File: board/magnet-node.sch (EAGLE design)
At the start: 19 parts, among them X1 SMA-142-0701-801/806

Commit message: started pcb
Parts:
- added C10, C11, C9: (no value), rcl:C-EUC0603
- added LED1: (no value), led:LEDSMT1206
- added R1, R2, R3: (no value), rcl:R-EU_R0603
- added SV2, SV3: (no value), con-lstb:MA07-1
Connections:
- removed net N$1: SV1.4, U$1.RST
- new net N$12: C10.2, R2.2, SV3.1, SV3.2, SV3.3, SV3.4, SV3.5, SV3.6, SV3.7, U$1.P1.3
- new net N$13: C11.2, LED1.A, R1.2, U$1.P1.5
- new net N$15: C9.2, R3.1, SV1.4, U$1.RST
- net +3V3: now also LED1.C, R3.2, SV2.1, SV2.2, SV2.3, SV2.4, SV2.5, SV2.6, SV2.7
- net GND: now also C10.1, C11.1, C9.1, R1.1, R2.1
- net N$6: now also U$2.SDA
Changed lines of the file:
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@@
 <?xml version="1.0" encoding="utf-8"?>
 <!DOCTYPE eagle SYSTEM "eagle.dtd">
-<eagle version="7.1.0">
+<eagle version="6.5.0">
 <drawing>
 <settings>
@@
 <part name="X1" library="con-coax" deviceset="SMA-" device="142-0701-801/806"/>
 <part name="GND13" library="supply1" deviceset="GND" device=""/>
+<part name="SV2" library="con-lstb" deviceset="MA07-1" device=""/>
+<part name="SV3" library="con-lstb" deviceset="MA07-1" device=""/>
+<part name="R1" library="rcl" deviceset="R-EU_" device="R0603"/>
+<part name="R2" library="rcl" deviceset="R-EU_" device="R0603"/>
+<part name="LED1" library="led" deviceset="LED" device="SMT1206"/>
+<part name="+3V6" library="supply1" deviceset="+3V3" device=""/>
+<part name="GND14" library="supply1" deviceset="GND" device=""/>
+<part name="GND15" library="supply1" deviceset="GND" device=""/>
+<part name="+3V7" library="supply1" deviceset="+3V3" device=""/>
+<part name="R3" library="rcl" deviceset="R-EU_" device="R0603"/>
+<part name="C9" library="rcl" deviceset="C-EU" device="C0603"/>
+<part name="GND16" library="supply1" deviceset="GND" device=""/>
+<part name="+3V8" library="supply1" deviceset="+3V3" device=""/>
+<part name="C10" library="rcl" deviceset="C-EU" device="C0603"/>
+<part name="C11" library="rcl" deviceset="C-EU" device="C0603"/>
 </parts>
 <sheets>
@@
 <instance part="X1" gate="G1" x="205.74" y="45.72" rot="MR0"/>
 <instance part="GND13" gate="1" x="203.2" y="40.64"/>
+<instance part="SV2" gate="1" x="86.36" y="81.28" rot="R180"/>
+<instance part="SV3" gate="1" x="88.9" y="81.28"/>
+<instance part="R1" gate="G$1" x="68.58" y="22.86" rot="R90"/>
+<instance part="R2" gate="G$1" x="73.66" y="22.86" rot="R90"/>
+<instance part="LED1" gate="G$1" x="68.58" y="58.42" rot="R180"/>
+<instance part="+3V6" gate="G$1" x="68.58" y="68.58"/>
+<instance part="GND14" gate="1" x="73.66" y="15.24"/>
+<instance part="GND15" gate="1" x="68.58" y="15.24"/>
+<instance part="+3V7" gate="G$1" x="78.74" y="96.52"/>
+<instance part="R3" gate="G$1" x="15.24" y="58.42" rot="R90"/>
+<instance part="C9" gate="G$1" x="15.24" y="38.1" rot="R180"/>
+<instance part="GND16" gate="1" x="15.24" y="33.02"/>
+<instance part="+3V8" gate="G$1" x="15.24" y="66.04"/>
+<instance part="C10" gate="G$1" x="78.74" y="22.86" rot="R180"/>
+<instance part="C11" gate="G$1" x="63.5" y="22.86" rot="R180"/>
 </instances>
 <busses>
@@
 <pinref part="GND13" gate="1" pin="GND"/>
 </segment>
+<segment>
+<pinref part="R2" gate="G$1" pin="1"/>
+<pinref part="GND14" gate="1" pin="GND"/>
+<pinref part="C10" gate="G$1" pin="1"/>
+<wire x1="78.74" y1="20.32" x2="78.74" y2="17.78" width="0.1524" layer="91"/>
+<wire x1="78.74" y1="17.78" x2="73.66" y2="17.78" width="0.1524" layer="91"/>
+<junction x="73.66" y="17.78"/>
+</segment>
+<segment>
+<pinref part="R1" gate="G$1" pin="1"/>
+<pinref part="GND15" gate="1" pin="GND"/>
+<pinref part="C11" gate="G$1" pin="1"/>
+<wire x1="63.5" y1="20.32" x2="63.5" y2="17.78" width="0.1524" layer="91"/>
+<wire x1="63.5" y1="17.78" x2="68.58" y2="17.78" width="0.1524" layer="91"/>
+<junction x="68.58" y="17.78"/>
+</segment>
+<segment>
+<pinref part="C9" gate="G$1" pin="1"/>
+<pinref part="GND16" gate="1" pin="GND"/>
+</segment>
 </net>
 <net name="+3V3" class="0">
@@
 <pinref part="+3V5" gate="G$1" pin="+3V3"/>
 </segment>
-</net>
-<net name="N$1" class="0">
-<segment>
-<pinref part="U$1" gate="G$1" pin="RST"/>
-<wire x1="25.4" y1="48.26" x2="22.86" y2="48.26" width="0.1524" layer="91"/>
-<wire x1="22.86" y1="48.26" x2="22.86" y2="50.8" width="0.1524" layer="91"/>
-<wire x1="22.86" y1="50.8" x2="5.08" y2="50.8" width="0.1524" layer="91"/>
-<pinref part="SV1" gate="1" pin="4"/>
+<segment>
+<pinref part="+3V6" gate="G$1" pin="+3V3"/>
+<pinref part="LED1" gate="G$1" pin="C"/>
+<wire x1="68.58" y1="66.04" x2="68.58" y2="63.5" width="0.1524" layer="91"/>
+</segment>
+<segment>
+<pinref part="SV2" gate="1" pin="7"/>
+<wire x1="78.74" y1="73.66" x2="78.74" y2="76.2" width="0.1524" layer="91"/>
+<pinref part="SV2" gate="1" pin="6"/>
+<junction x="78.74" y="76.2"/>
+<wire x1="78.74" y1="76.2" x2="78.74" y2="78.74" width="0.1524" layer="91"/>
+<pinref part="SV2" gate="1" pin="5"/>
+<junction x="78.74" y="78.74"/>
+<wire x1="78.74" y1="78.74" x2="78.74" y2="81.28" width="0.1524" layer="91"/>
+<pinref part="SV2" gate="1" pin="4"/>
+<junction x="78.74" y="81.28"/>
+<wire x1="78.74" y1="81.28" x2="78.74" y2="83.82" width="0.1524" layer="91"/>
+<pinref part="SV2" gate="1" pin="3"/>
+<junction x="78.74" y="83.82"/>
+<wire x1="78.74" y1="83.82" x2="78.74" y2="86.36" width="0.1524" layer="91"/>
+<pinref part="SV2" gate="1" pin="2"/>
+<junction x="78.74" y="86.36"/>
+<wire x1="78.74" y1="86.36" x2="78.74" y2="88.9" width="0.1524" layer="91"/>
+<pinref part="SV2" gate="1" pin="1"/>
+<junction x="78.74" y="88.9"/>
+<wire x1="78.74" y1="88.9" x2="78.74" y2="93.98" width="0.1524" layer="91"/>
+<pinref part="+3V7" gate="G$1" pin="+3V3"/>
+</segment>
+<segment>
+<pinref part="R3" gate="G$1" pin="2"/>
+<pinref part="+3V8" gate="G$1" pin="+3V3"/>
 </segment>
 </net>
@@
 <net name="N$6" class="0">
 <segment>
-<wire x1="83.82" y1="45.72" x2="127" y2="45.72" width="0.1524" layer="91"/>
+<wire x1="83.82" y1="45.72" x2="121.92" y2="45.72" width="0.1524" layer="91"/>
+<wire x1="121.92" y1="45.72" x2="124.46" y2="45.72" width="0.1524" layer="91"/>
 <wire x1="83.82" y1="33.02" x2="83.82" y2="45.72" width="0.1524" layer="91"/>
 <pinref part="U$1" gate="G$1" pin="P1.7"/>
 <wire x1="63.5" y1="33.02" x2="83.82" y2="33.02" width="0.1524" layer="91"/>
+<pinref part="U$2" gate="G$1" pin="SDA"/>
+<wire x1="127" y1="45.72" x2="124.46" y2="45.72" width="0.1524" layer="91"/>
 </segment>
 </net>
@@
 </segment>
 </net>
+<net name="N$12" class="0">
+<segment>
+<pinref part="SV3" gate="1" pin="7"/>
+<wire x1="96.52" y1="88.9" x2="96.52" y2="86.36" width="0.1524" layer="91"/>
+<pinref part="SV3" gate="1" pin="6"/>
+<junction x="96.52" y="86.36"/>
+<wire x1="96.52" y1="86.36" x2="96.52" y2="83.82" width="0.1524" layer="91"/>
+<pinref part="SV3" gate="1" pin="5"/>
+<junction x="96.52" y="83.82"/>
+<wire x1="96.52" y1="83.82" x2="96.52" y2="81.28" width="0.1524" layer="91"/>
+<pinref part="SV3" gate="1" pin="4"/>
+<junction x="96.52" y="81.28"/>
+<wire x1="96.52" y1="81.28" x2="96.52" y2="78.74" width="0.1524" layer="91"/>
+<pinref part="SV3" gate="1" pin="3"/>
+<junction x="96.52" y="78.74"/>
+<wire x1="96.52" y1="78.74" x2="96.52" y2="76.2" width="0.1524" layer="91"/>
+<pinref part="SV3" gate="1" pin="2"/>
+<junction x="96.52" y="76.2"/>
+<wire x1="96.52" y1="76.2" x2="96.52" y2="73.66" width="0.1524" layer="91"/>
+<pinref part="SV3" gate="1" pin="1"/>
+<junction x="96.52" y="73.66"/>
+<pinref part="R2" gate="G$1" pin="2"/>
+<wire x1="73.66" y1="27.94" x2="73.66" y2="30.48" width="0.1524" layer="91"/>
+<wire x1="73.66" y1="30.48" x2="73.66" y2="43.18" width="0.1524" layer="91"/>
+<wire x1="73.66" y1="43.18" x2="73.66" y2="58.42" width="0.1524" layer="91"/>
+<wire x1="73.66" y1="58.42" x2="96.52" y2="58.42" width="0.1524" layer="91"/>
+<wire x1="96.52" y1="58.42" x2="96.52" y2="73.66" width="0.1524" layer="91"/>
+<pinref part="U$1" gate="G$1" pin="P1.3"/>
+<wire x1="63.5" y1="43.18" x2="73.66" y2="43.18" width="0.1524" layer="91"/>
+<junction x="73.66" y="43.18"/>
+<pinref part="C10" gate="G$1" pin="2"/>
+<wire x1="78.74" y1="27.94" x2="78.74" y2="30.48" width="0.1524" layer="91"/>
+<wire x1="78.74" y1="30.48" x2="73.66" y2="30.48" width="0.1524" layer="91"/>
+<junction x="73.66" y="30.48"/>
+</segment>
+</net>
+<net name="N$13" class="0">
+<segment>
+<pinref part="LED1" gate="G$1" pin="A"/>
+<pinref part="R1" gate="G$1" pin="2"/>
+<wire x1="68.58" y1="55.88" x2="68.58" y2="38.1" width="0.1524" layer="91"/>
+<wire x1="68.58" y1="38.1" x2="68.58" y2="30.48" width="0.1524" layer="91"/>
+<wire x1="68.58" y1="30.48" x2="68.58" y2="27.94" width="0.1524" layer="91"/>
+<pinref part="C11" gate="G$1" pin="2"/>
+<wire x1="63.5" y1="27.94" x2="63.5" y2="30.48" width="0.1524" layer="91"/>
+<wire x1="63.5" y1="30.48" x2="68.58" y2="30.48" width="0.1524" layer="91"/>
+<junction x="68.58" y="30.48"/>
+<pinref part="U$1" gate="G$1" pin="P1.5"/>
+<wire x1="63.5" y1="38.1" x2="68.58" y2="38.1" width="0.1524" layer="91"/>
+<junction x="68.58" y="38.1"/>
+</segment>
+</net>
+<net name="N$15" class="0">
+<segment>
+<pinref part="C9" gate="G$1" pin="2"/>
+<pinref part="R3" gate="G$1" pin="1"/>
+<wire x1="15.24" y1="43.18" x2="15.24" y2="50.8" width="0.1524" layer="91"/>
+<pinref part="U$1" gate="G$1" pin="RST"/>
+<wire x1="25.4" y1="48.26" x2="22.86" y2="48.26" width="0.1524" layer="91"/>
+<wire x1="22.86" y1="48.26" x2="22.86" y2="50.8" width="0.1524" layer="91"/>
+<wire x1="22.86" y1="50.8" x2="15.24" y2="50.8" width="0.1524" layer="91"/>
+<pinref part="SV1" gate="1" pin="4"/>
+<wire x1="15.24" y1="50.8" x2="5.08" y2="50.8" width="0.1524" layer="91"/>
+<wire x1="15.24" y1="53.34" x2="15.24" y2="50.8" width="0.1524" layer="91"/>
+<junction x="15.24" y="50.8"/>
+</segment>
+</net>

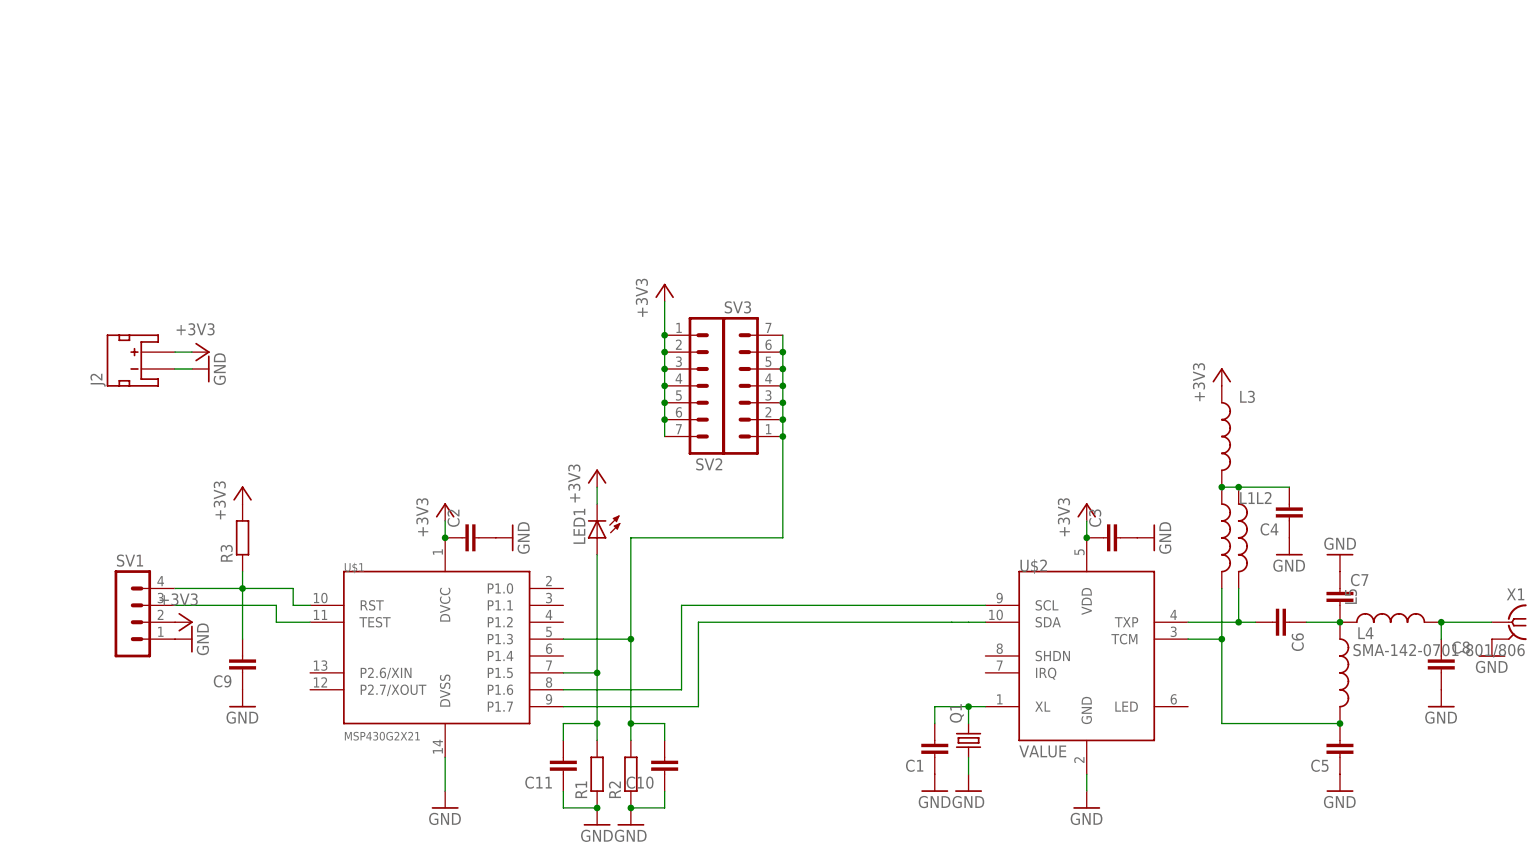
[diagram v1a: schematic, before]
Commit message: initial route
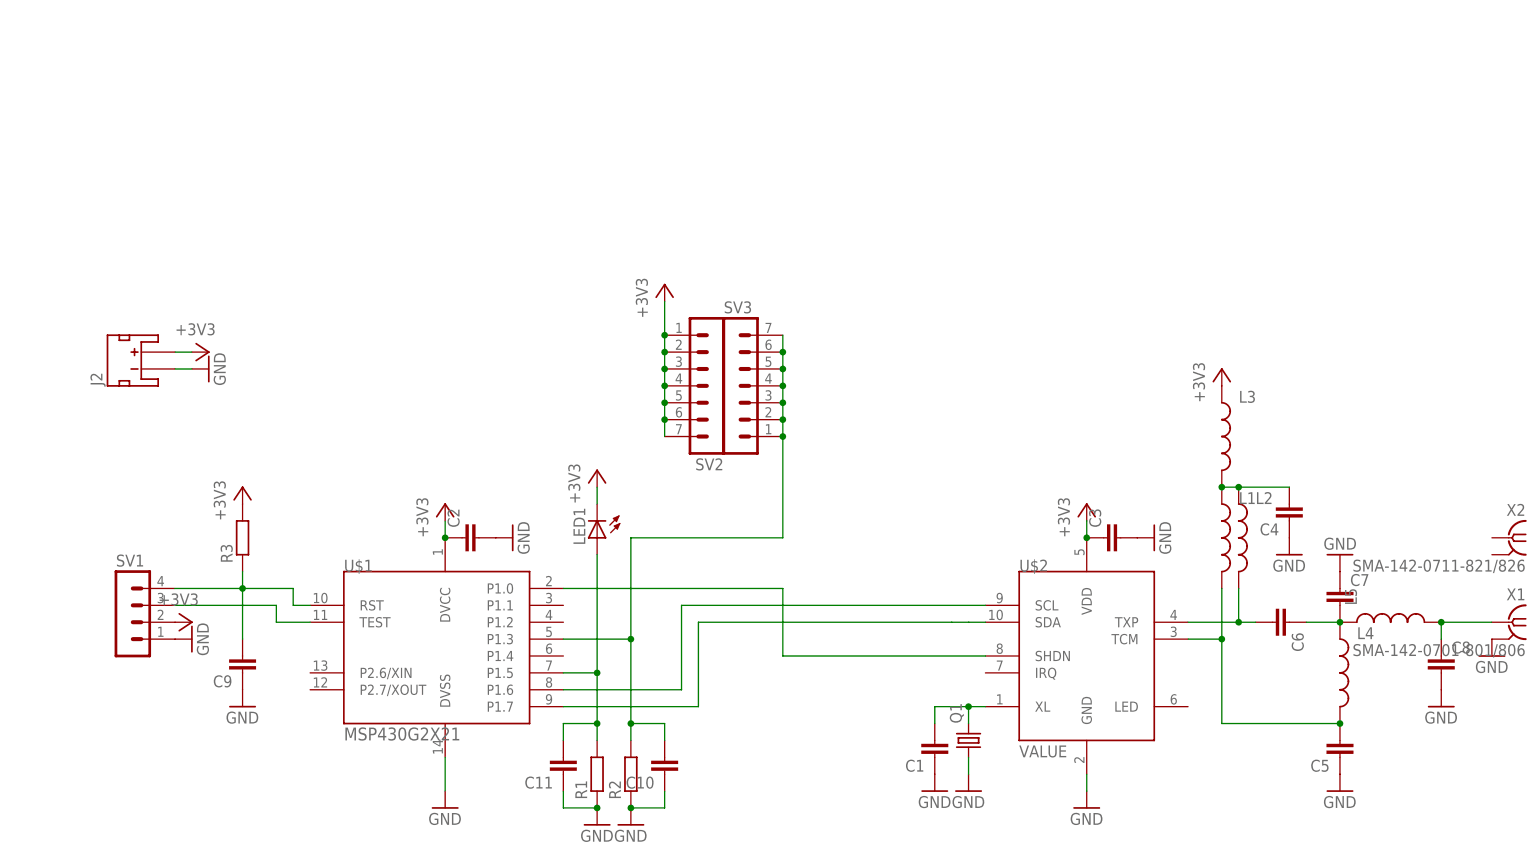
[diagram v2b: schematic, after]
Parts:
- added X2: SMA-142-0711-821/826, con-coax:SMA-142-0711-821/826
- SV2, SV3: device con-lstb:MA07-1 -> Mine:MA07-1S
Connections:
- new net N$1: U$1.P1.0, U$2.SHDN
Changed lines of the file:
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@@
 <part name="X1" library="con-coax" deviceset="SMA-" device="142-0701-801/806"/>
 <part name="GND13" library="supply1" deviceset="GND" device=""/>
-<part name="SV2" library="con-lstb" deviceset="MA07-1" device=""/>
-<part name="SV3" library="con-lstb" deviceset="MA07-1" device=""/>
+<part name="SV2" library="Mine" deviceset="MA07-1" device="S"/>
+<part name="SV3" library="Mine" deviceset="MA07-1" device="S"/>
 <part name="R1" library="rcl" deviceset="R-EU_" device="R0603"/>
 <part name="R2" library="rcl" deviceset="R-EU_" device="R0603"/>
@@
 <part name="C10" library="rcl" deviceset="C-EU" device="C0603"/>
 <part name="C11" library="rcl" deviceset="C-EU" device="C0603"/>
+<part name="X2" library="con-coax" deviceset="SMA-" device="142-0711-821/826"/>
 </parts>
 <sheets>
@@
 <instance part="C10" gate="G$1" x="78.74" y="22.86" rot="R180"/>
 <instance part="C11" gate="G$1" x="63.5" y="22.86" rot="R180"/>
+<instance part="X2" gate="G1" x="205.74" y="58.42" rot="MR0"/>
 </instances>
 <busses>
@@
 </segment>
 </net>
+<net name="N$1" class="0">
+<segment>
+<pinref part="U$2" gate="G$1" pin="SHDN"/>
+<wire x1="127" y1="40.64" x2="96.52" y2="40.64" width="0.1524" layer="91"/>
+<pinref part="U$1" gate="G$1" pin="P1.0"/>
+<wire x1="63.5" y1="50.8" x2="96.52" y2="50.8" width="0.1524" layer="91"/>
+<wire x1="96.52" y1="50.8" x2="96.52" y2="40.64" width="0.1524" layer="91"/>
+</segment>
+</net>

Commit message: changing sensor power arragment
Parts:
- added LED2: (no value), led:LEDSMT1206
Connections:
- new net VCCS: LED1.C, LED2.C, SV2.1, SV2.2, SV2.3, SV2.4, SV2.5, SV2.6, SV2.7, U$1.P1.4
- net +3V3: no longer LED1.C, SV2.1, SV2.2, SV2.3, SV2.4, SV2.5, SV2.6, SV2.7
- net N$13: now also LED2.A
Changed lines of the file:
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@@
 <part name="R2" library="rcl" deviceset="R-EU_" device="R0603"/>
 <part name="LED1" library="led" deviceset="LED" device="SMT1206"/>
-<part name="+3V6" library="supply1" deviceset="+3V3" device=""/>
 <part name="GND14" library="supply1" deviceset="GND" device=""/>
 <part name="GND15" library="supply1" deviceset="GND" device=""/>
-<part name="+3V7" library="supply1" deviceset="+3V3" device=""/>
 <part name="R3" library="rcl" deviceset="R-EU_" device="R0603"/>
 <part name="C9" library="rcl" deviceset="C-EU" device="C0603"/>
@@
 <part name="C11" library="rcl" deviceset="C-EU" device="C0603"/>
 <part name="X2" library="con-coax" deviceset="SMA-" device="142-0711-821/826"/>
+<part name="LED2" library="led" deviceset="LED" device="SMT1206"/>
 </parts>
 <sheets>
@@
 <instance part="R2" gate="G$1" x="73.66" y="22.86" rot="R90"/>
 <instance part="LED1" gate="G$1" x="68.58" y="58.42" rot="R180"/>
-<instance part="+3V6" gate="G$1" x="68.58" y="68.58"/>
 <instance part="GND14" gate="1" x="73.66" y="15.24"/>
 <instance part="GND15" gate="1" x="68.58" y="15.24"/>
-<instance part="+3V7" gate="G$1" x="78.74" y="96.52"/>
 <instance part="R3" gate="G$1" x="15.24" y="58.42" rot="R90"/>
 <instance part="C9" gate="G$1" x="15.24" y="38.1" rot="R180"/>
@@
 <instance part="C11" gate="G$1" x="63.5" y="22.86" rot="R180"/>
 <instance part="X2" gate="G1" x="205.74" y="58.42" rot="MR0"/>
+<instance part="LED2" gate="G$1" x="63.5" y="58.42" rot="R180"/>
 </instances>
 <busses>
@@
 <pinref part="L3" gate="G$1" pin="1"/>
 <pinref part="+3V5" gate="G$1" pin="+3V3"/>
-</segment>
-<segment>
-<pinref part="+3V6" gate="G$1" pin="+3V3"/>
-<pinref part="LED1" gate="G$1" pin="C"/>
-<wire x1="68.58" y1="66.04" x2="68.58" y2="63.5" width="0.1524" layer="91"/>
-</segment>
-<segment>
-<pinref part="SV2" gate="1" pin="7"/>
-<wire x1="78.74" y1="73.66" x2="78.74" y2="76.2" width="0.1524" layer="91"/>
-<pinref part="SV2" gate="1" pin="6"/>
-<junction x="78.74" y="76.2"/>
-<wire x1="78.74" y1="76.2" x2="78.74" y2="78.74" width="0.1524" layer="91"/>
-<pinref part="SV2" gate="1" pin="5"/>
-<junction x="78.74" y="78.74"/>
-<wire x1="78.74" y1="78.74" x2="78.74" y2="81.28" width="0.1524" layer="91"/>
-<pinref part="SV2" gate="1" pin="4"/>
-<junction x="78.74" y="81.28"/>
-<wire x1="78.74" y1="81.28" x2="78.74" y2="83.82" width="0.1524" layer="91"/>
-<pinref part="SV2" gate="1" pin="3"/>
-<junction x="78.74" y="83.82"/>
-<wire x1="78.74" y1="83.82" x2="78.74" y2="86.36" width="0.1524" layer="91"/>
-<pinref part="SV2" gate="1" pin="2"/>
-<junction x="78.74" y="86.36"/>
-<wire x1="78.74" y1="86.36" x2="78.74" y2="88.9" width="0.1524" layer="91"/>
-<pinref part="SV2" gate="1" pin="1"/>
-<junction x="78.74" y="88.9"/>
-<wire x1="78.74" y1="88.9" x2="78.74" y2="93.98" width="0.1524" layer="91"/>
-<pinref part="+3V7" gate="G$1" pin="+3V3"/>
 </segment>
 <segment>
@@
 <wire x1="63.5" y1="38.1" x2="68.58" y2="38.1" width="0.1524" layer="91"/>
 <junction x="68.58" y="38.1"/>
+<pinref part="LED2" gate="G$1" pin="A"/>
+<wire x1="63.5" y1="55.88" x2="68.58" y2="55.88" width="0.1524" layer="91"/>
+<junction x="68.58" y="55.88"/>
 </segment>
 </net>
@@
 </segment>
 </net>
+<net name="VCCS" class="0">
+<segment>
+<pinref part="SV2" gate="1" pin="7"/>
+<wire x1="78.74" y1="73.66" x2="78.74" y2="76.2" width="0.1524" layer="91"/>
+<pinref part="SV2" gate="1" pin="6"/>
+<junction x="78.74" y="76.2"/>
+<wire x1="78.74" y1="76.2" x2="78.74" y2="78.74" width="0.1524" layer="91"/>
+<pinref part="SV2" gate="1" pin="5"/>
+<junction x="78.74" y="78.74"/>
+<wire x1="78.74" y1="78.74" x2="78.74" y2="81.28" width="0.1524" layer="91"/>
+<pinref part="SV2" gate="1" pin="4"/>
+<junction x="78.74" y="81.28"/>
+<wire x1="78.74" y1="81.28" x2="78.74" y2="83.82" width="0.1524" layer="91"/>
+<pinref part="SV2" gate="1" pin="3"/>
+<junction x="78.74" y="83.82"/>
+<wire x1="78.74" y1="83.82" x2="78.74" y2="86.36" width="0.1524" layer="91"/>
+<pinref part="SV2" gate="1" pin="2"/>
+<junction x="78.74" y="86.36"/>
+<wire x1="78.74" y1="86.36" x2="78.74" y2="88.9" width="0.1524" layer="91"/>
+<pinref part="SV2" gate="1" pin="1"/>
+<junction x="78.74" y="88.9"/>
+<wire x1="78.74" y1="88.9" x2="78.74" y2="93.98" width="0.1524" layer="91"/>
+<label x="78.74" y="93.98" size="1.778" layer="95" rot="R90" xref="yes"/>
+</segment>
+<segment>
+<pinref part="LED1" gate="G$1" pin="C"/>
+<wire x1="68.58" y1="66.04" x2="68.58" y2="63.5" width="0.1524" layer="91"/>
+<pinref part="LED2" gate="G$1" pin="C"/>
+<wire x1="63.5" y1="63.5" x2="68.58" y2="63.5" width="0.1524" layer="91"/>
+<label x="68.58" y="66.04" size="1.778" layer="95" rot="R90" xref="yes"/>
+<junction x="68.58" y="63.5"/>
+</segment>
+<segment>
+<pinref part="U$1" gate="G$1" pin="P1.4"/>
+<wire x1="63.5" y1="40.64" x2="66.04" y2="40.64" width="0.1524" layer="91"/>
+<label x="66.04" y="40.64" size="1.778" layer="95" xref="yes"/>
+</segment>
+</net>
